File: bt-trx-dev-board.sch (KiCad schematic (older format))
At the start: 12 parts, among them J1 RJ45, J2 PTT_BUTTON, J3 PTT_CON, J5 PTT_SELECT, U1 SILabs_WT32i

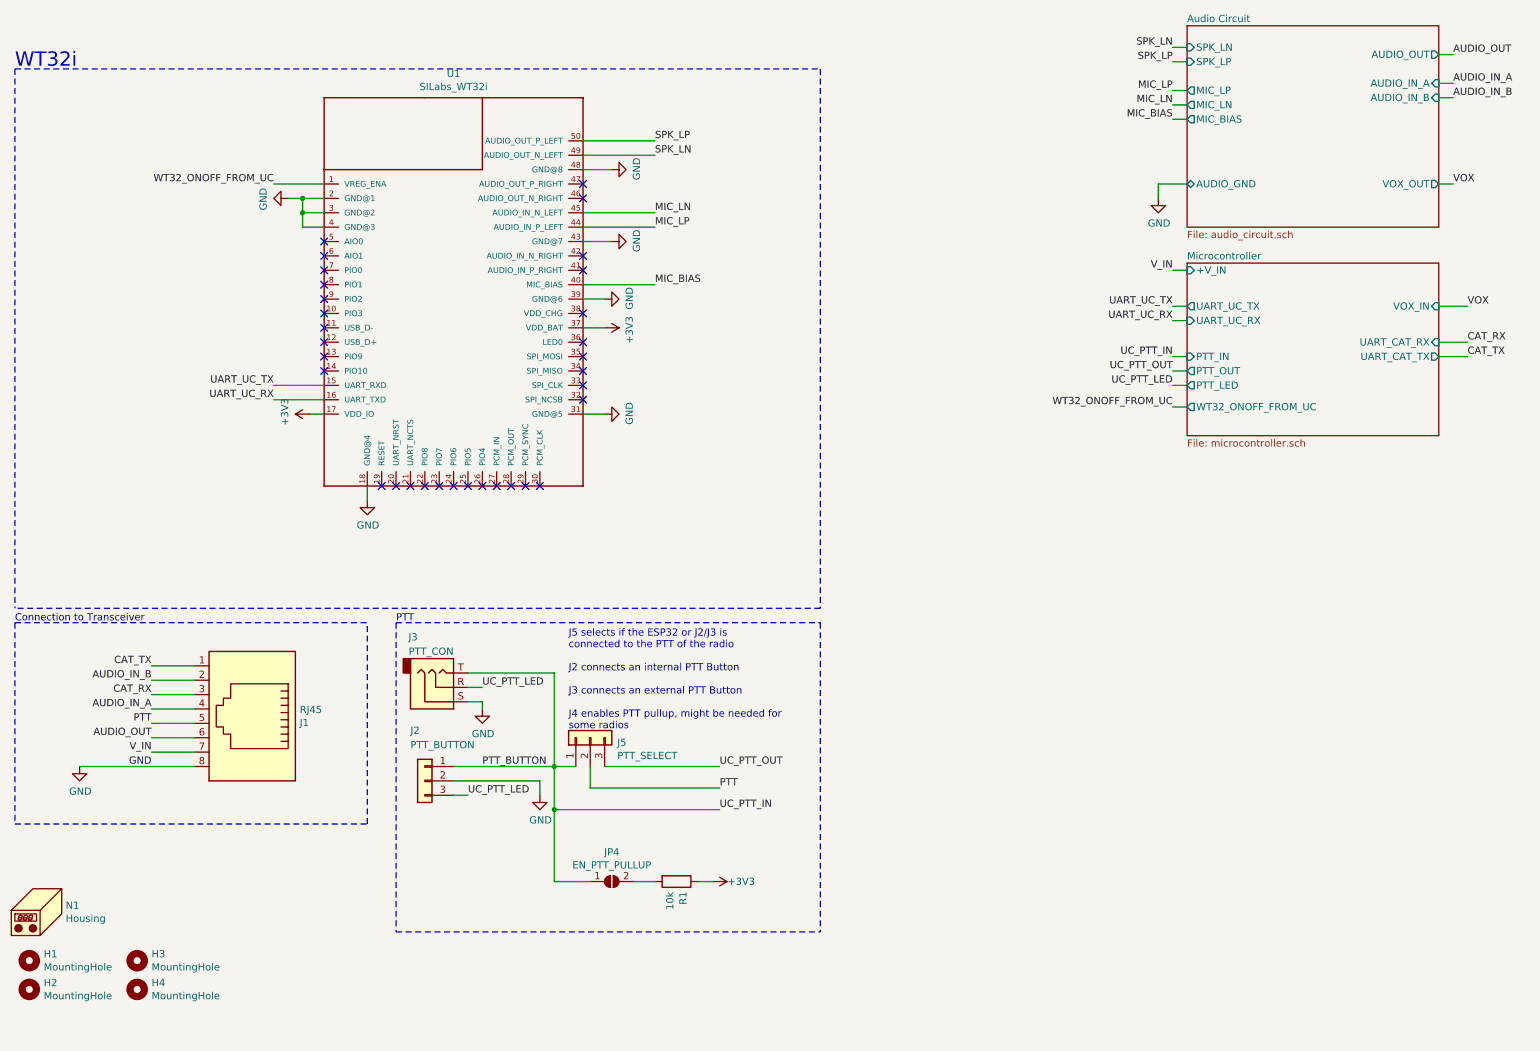
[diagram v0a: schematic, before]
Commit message: [#22] Insert Optocoupler for PTT
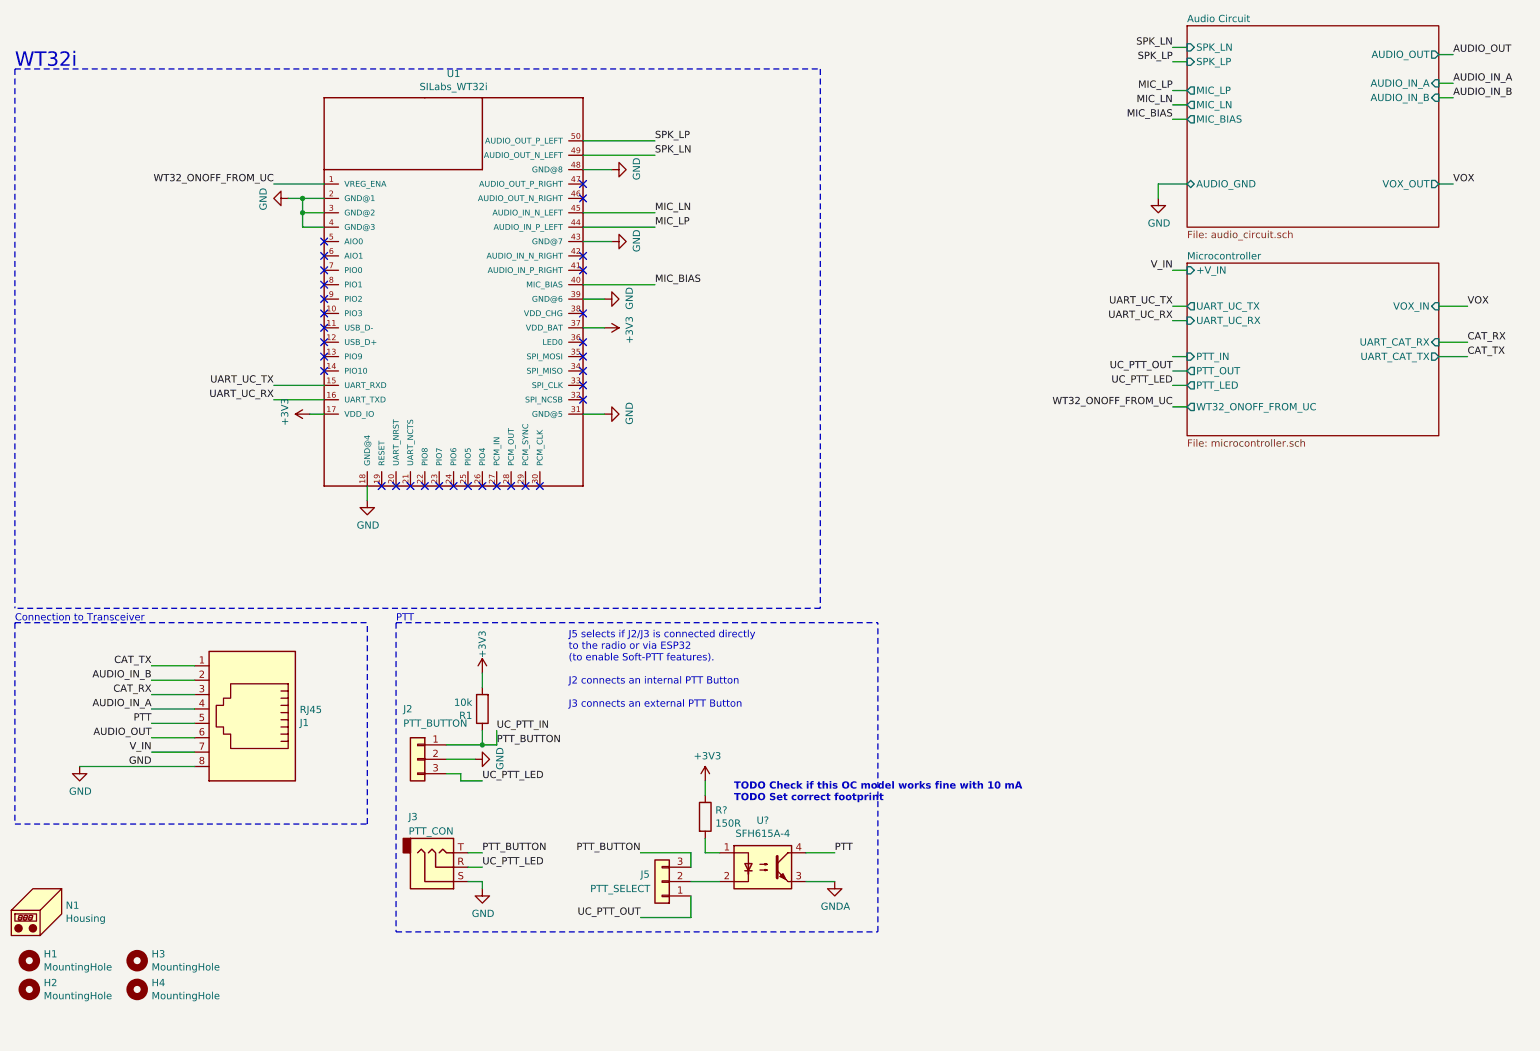
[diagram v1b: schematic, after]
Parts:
- removed JP4: EN_PTT_PULLUP, Jumper:SolderJumper-2_P1.3mm_Open_TrianglePad1.0x1.5mm, symbol Jumper:SolderJumper_2_Open
- added R?: 150R, Resistor_SMD:R_0805_2012Metric_Pad1.15x1.40mm_HandSolder, symbol Device:R
- added U?: SFH615A-4, Package_DIP:DIP-4_W7.62mm, symbol Isolator:SFH617A-1
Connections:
- net +3V3: now also R1.2, R?.1; no longer R1.1
- net PTT: now also U?.4; no longer J5.2 (Pin_2)
- net PTT_BUTTON: now also J5.3 (Pin_3), R1.1; no longer J5.1 (Pin_1)
- net UC_PTT_OUT: now also J5.1 (Pin_1); no longer J5.3 (Pin_3)
- new net: J5.2 (Pin_2), U?.2
- new net: R?.2, U?.1
- new net GNDA: U?.3
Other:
- note added: "J5 selects if J2/J3 is connected directly\nto the radio or via ESP32\n(to enable Soft-PTT features).\n\nJ2 connects an internal PTT Button\n\nJ3 connects an external PTT Button"
- note added: "TODO Check if this OC model works fine with 10 mA\nTODO Set correct footprint"
- note removed: "J5 selects if the ESP32 or J2/J3 is\nconnected to the PTT of the radio\n\nJ2 connects an internal PTT Button\n\nJ3 connects an external PTT Button\n\nJ4 enables PTT pullup, might be needed for\nsome radios"
- moved on the sheet: J2, J3, J5, R1
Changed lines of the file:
@@
 Sheet 1 3
 Title "BT-TRX Development Board "
-Date "2019-09-28"
-Rev "v4.1"
+Date "2020-01-04"
+Rev "v5.0"
 Comp "bt-trx.com"
 Comment1 "Licensed under CERN OHL v1.2 - https://ohwr.org/licenses/cern-ohl/v1.2"
@@
 L power:GND #PWR05
 U 1 1 5C0EA10B
-P 4350 6000
-F 0 "#PWR05" H 4350 5750 50  0001 C CNN
-F 1 "GND" H 4355 5827 50  0000 C CNN
-F 2 "" H 4350 6000 50  0001 C CNN
-F 3 "" H 4350 6000 50  0001 C CNN
-	1    4350 6000
-	1    0    0    -1
+P 3900 5750
+F 0 "#PWR05" H 3900 5500 50  0001 C CNN
+F 1 "GND" H 3905 5577 50  0000 C CNN
+F 2 "" H 3900 5750 50  0001 C CNN
+F 3 "" H 3900 5750 50  0001 C CNN
+	1    3900 5750
+	0    -1   -1   0
 $EndComp
 $Comp
@@
 L Connector_Generic:Conn_01x03 J5
 U 1 1 5C7B53A0
-P 4700 5600
-F 0 "J5" V 4666 5412 50  0000 R CNN
-F 1 "PTT_SELECT" V 4575 5412 50  0000 R CNN
-F 2 "Connector_PinHeader_2.54mm:PinHeader_1x03_P2.54mm_Vertical" H 4700 5600 50  0001 C CNN
-F 3 "~" H 4700 5600 50  0001 C CNN
-F 4 "855-M20-9990346" H -2200 -200 50  0001 C CNN "Mouser Best.Nr."
-	1    4700 5600
-	0    -1   -1   0
-$EndComp
-Wire Wire Line
-	4800 5800 5600 5800
-Text Label 5600 5800 0    50   ~ 0
+P 5200 6600
+F 0 "J5" H 5350 6550 50  0000 R CNN
+F 1 "PTT_SELECT" H 5700 6650 50  0000 R CNN
+F 2 "Connector_PinHeader_2.54mm:PinHeader_1x03_P2.54mm_Vertical" H 5200 6600 50  0001 C CNN
+F 3 "~" H 5200 6600 50  0001 C CNN
+F 4 "855-M20-9990346" H -1700 800 50  0001 C CNN "Mouser Best.Nr."
+	1    5200 6600
+	-1   0    0    1
+$EndComp
+Text Label 5050 6850 2    50   ~ 0
 UC_PTT_OUT
-Wire Wire Line
-	4700 5800 4700 5950
-Wire Wire Line
-	4700 5950 5600 5950
-Text Label 5600 5950 0    50   ~ 0
+Text Label 6400 6400 0    50   ~ 0
 PTT
-Text Label 3950 5800 0    50   ~ 0
+Text Label 4050 5650 0    50   ~ 0
 PTT_BUTTON
 $Sheet
@@
 Wire Wire Line
 	8850 3050 8750 3050
-Text Label 8750 2950 2    50   ~ 0
-UC_PTT_IN
 Text Label 8750 3050 2    50   ~ 0
 UC_PTT_OUT
-Connection ~ 4450 5800
-Wire Wire Line
-	4450 5800 4600 5800
 $Comp
 L power:GND #PWR06
 U 1 1 5C7A36F0
-P 3950 5400
-F 0 "#PWR06" H 3950 5150 50  0001 C CNN
-F 1 "GND" H 3955 5227 50  0000 C CNN
-F 2 "" H 3950 5400 50  0001 C CNN
-F 3 "" H 3950 5400 50  0001 C CNN
-	1    3950 5400
-	1    0    0    -1
-$EndComp
-Wire Wire Line
-	3950 5350 3950 5400
-Wire Wire Line
-	3850 5350 3950 5350
-Wire Wire Line
-	4450 5150 4450 5800
+P 3950 6650
+F 0 "#PWR06" H 3950 6400 50  0001 C CNN
+F 1 "GND" H 3955 6477 50  0000 C CNN
+F 2 "" H 3950 6650 50  0001 C CNN
+F 3 "" H 3950 6650 50  0001 C CNN
+	1    3950 6650
+	1    0    0    -1
+$EndComp
+Wire Wire Line
+	3950 6600 3950 6650
+Wire Wire Line
+	3850 6600 3950 6600
 $Comp
 L power:GND #PWR01
@@
 L power:+3V3 #PWR012
 U 1 1 5CD1BCEE
-P 5550 6600
+P 3950 5150
 AR Path="/5CD1BCEE" Ref="#PWR012"  Part="1"
 AR Path="/5C10B93A/5CD1BCEE" Ref="#PWR?"  Part="1"
-F 0 "#PWR012" H 5550 6450 50  0001 C CNN
-F 1 "+3V3" V 5550 6800 50  0000 C CNN
-F 2 "" H 5550 6600 50  0001 C CNN
-F 3 "" H 5550 6600 50  0001 C CNN
-	1    5550 6600
-	0    1    1    0
+F 0 "#PWR012" H 3950 5000 50  0001 C CNN
+F 1 "+3V3" V 3950 5350 50  0000 C CNN
+F 2 "" H 3950 5150 50  0001 C CNN
+F 3 "" H 3950 5150 50  0001 C CNN
+	1    3950 5150
+	1    0    0    -1
 $EndComp
 $Comp
 L Device:R R1
 U 1 1 5CD1BCF6
-P 5300 6600
+P 3950 5400
 AR Path="/5CD1BCF6" Ref="R1"  Part="1"
 AR Path="/5C10B93A/5CD1BCF6" Ref="R?"  Part="1"
-F 0 "R1" H 5370 6646 50  0000 L CNN
-F 1 "10k" H 5370 6555 50  0000 L CNN
-F 2 "Resistor_SMD:R_0805_2012Metric_Pad1.15x1.40mm_HandSolder" V 5230 6600 50  0001 C CNN
-F 3 "~" H 5300 6600 50  0001 C CNN
-F 4 " 603-RC0805FR-0710KL" H 1650 1450 50  0001 C CNN "Mouser Best.Nr."
-	1    5300 6600
-	0    1    1    0
-$EndComp
-Wire Wire Line
-	5550 6600 5450 6600
-Text Label 5600 6100 0    50   ~ 0
-UC_PTT_IN
-Text Notes 4550 5550 0    50   ~ 0
-J5 selects if the ESP32 or J2/J3 is\nconnected to the PTT of the radio\n\nJ2 connects an internal PTT Button\n\nJ3 connects an external PTT Button\n\nJ4 enables PTT pullup, might be needed for\nsome radios
-Wire Notes Line
-	3350 6950 6300 6950
-Wire Notes Line
-	3350 4800 6300 4800
+F 0 "R1" H 4020 5446 50  0000 L CNN
+F 1 "10k" H 4020 5355 50  0000 L CNN
+F 2 "Resistor_SMD:R_0805_2012Metric_Pad1.15x1.40mm_HandSolder" V 3880 5400 50  0001 C CNN
+F 3 "~" H 3950 5400 50  0001 C CNN
+F 4 " 603-RC0805FR-0710KL" H 300 250 50  0001 C CNN "Mouser Best.Nr."
+	1    3950 5400
+	-1   0    0    1
+$EndComp
+Text Notes 4550 5400 0    50   ~ 0
+J5 selects if J2/J3 is connected directly\nto the radio or via ESP32\n(to enable Soft-PTT features).\n\nJ2 connects an internal PTT Button\n\nJ3 connects an external PTT Button
 $Comp
 L Mechanical:MountingHole H3
@@
 	1    0    0    -1
 $EndComp
-Wire Wire Line
-	4450 5800 4450 6100
-Wire Wire Line
-	5600 6100 4450 6100
-Connection ~ 4450 6100
-Wire Wire Line
-	4450 6100 4450 6600
-Wire Notes Line
-	6300 4800 6300 6950
 Wire Notes Line
 	3350 4800 3350 6950
@@
 L Connector:AudioJack3 J3
 U 1 1 5D8E8C9D
-P 3650 5250
-F 0 "J3" H 3500 4900 50  0000 R CNN
-F 1 "PTT_CON" H 3750 5000 50  0000 R CNN
-F 2 "Connector_Audio:Jack_3.5mm_CUI_SJ1-3533NG_Horizontal" H 3650 5250 50  0001 C CNN
-F 3 "~" H 3650 5250 50  0001 C CNN
-F 4 "490-SJ1-3533NG" H 3650 5250 50  0001 C CNN "Mouser Best.Nr."
-	1    3650 5250
+P 3650 6500
+F 0 "J3" H 3500 6150 50  0000 R CNN
+F 1 "PTT_CON" H 3750 6250 50  0000 R CNN
+F 2 "Connector_Audio:Jack_3.5mm_CUI_SJ1-3533NG_Horizontal" H 3650 6500 50  0001 C CNN
+F 3 "~" H 3650 6500 50  0001 C CNN
+F 4 "490-SJ1-3533NG" H 3650 6500 50  0001 C CNN "Mouser Best.Nr."
+	1    3650 6500
 	1    0    0    1
 $EndComp
 Wire Wire Line
-	3850 5250 3950 5250
-Text Label 3950 5250 0    50   ~ 0
+	3850 6500 3950 6500
+Text Label 3950 6500 0    50   ~ 0
 UC_PTT_LED
 Wire Wire Line
@@
 UC_PTT_LED
 Wire Wire Line
-	3850 5150 4450 5150
-Wire Wire Line
-	3750 5800 4450 5800
-Wire Wire Line
 	10600 2600 10800 2600
 Text Label 10800 2600 0    50   ~ 0
@@
 VOX
 $Comp
-L Jumper:SolderJumper_2_Open JP4
-U 1 1 5D933957
-P 4850 6600
-F 0 "JP4" H 4850 6805 50  0000 C CNN
-F 1 "EN_PTT_PULLUP" H 4850 6714 50  0000 C CNN
-F 2 "Jumper:SolderJumper-2_P1.3mm_Open_TrianglePad1.0x1.5mm" H 4850 6600 50  0001 C CNN
-F 3 "~" H 4850 6600 50  0001 C CNN
-	1    4850 6600
-	1    0    0    -1
-$EndComp
-Wire Wire Line
-	4450 6600 4700 6600
-Wire Wire Line
-	5000 6600 5150 6600
-$Comp
 L Connector_Generic:Conn_01x03 J2
 U 1 1 5D9A6771
-P 3550 5900
-F 0 "J2" H 3650 6250 50  0000 R CNN
-F 1 "PTT_BUTTON" H 3650 6150 50  0000 R CNN
-F 2 "Connector_PinHeader_2.54mm:PinHeader_1x03_P2.54mm_Vertical" H 3550 5900 50  0001 C CNN
-F 3 "~" H 3550 5900 50  0001 C CNN
-F 4 "855-M20-9990346" H -3350 100 50  0001 C CNN "Mouser Best.Nr."
-	1    3550 5900
+P 3500 5750
+F 0 "J2" H 3600 6100 50  0000 R CNN
+F 1 "PTT_BUTTON" H 3600 6000 50  0000 R CNN
+F 2 "Connector_PinHeader_2.54mm:PinHeader_1x03_P2.54mm_Vertical" H 3500 5750 50  0001 C CNN
+F 3 "~" H 3500 5750 50  0001 C CNN
+F 4 "855-M20-9990346" H -3400 -50 50  0001 C CNN "Mouser Best.Nr."
+	1    3500 5750
 	-1   0    0    -1
 $EndComp
-Text Label 3850 6000 0    50   ~ 0
+Text Label 3950 5900 0    50   ~ 0
 UC_PTT_LED
-Wire Wire Line
-	4350 5900 4350 6000
-Wire Wire Line
-	3750 5900 4350 5900
-Wire Wire Line
-	3750 6000 3850 6000
+$Comp
+L Isolator:SFH617A-1 U?
+U 1 1 5E115F72
+P 5900 6500
+F 0 "U?" H 5900 6825 50  0000 C CNN
+F 1 "SFH615A-4" H 5900 6734 50  0000 C CNN
+F 2 "Package_DIP:DIP-4_W7.62mm" H 5700 6300 50  0001 L CIN
+F 3 "https://asset.conrad.com/media10/add/160267/c1/-/en/000183258DS01/datenblatt-183258-isocom-components-optokoppler-phototransistor-sfh615a-4xsm-smd-4-transistor-dc.pdf" H 5900 6500 50  0001 L CNN
+	1    5900 6500
+	1    0    0    -1
+$EndComp
+$Comp
+L power:+3V3 #PWR0102
+U 1 1 5E11C622
+P 5500 5900
+F 0 "#PWR0102" H 5500 5750 50  0001 C CNN
+F 1 "+3V3" H 5515 6073 50  0000 C CNN
+F 2 "" H 5500 5900 50  0001 C CNN
+F 3 "" H 5500 5900 50  0001 C CNN
+	1    5500 5900
+	1    0    0    -1
+$EndComp
+$Comp
+L Device:R R?
+U 1 1 5E1205EF
+P 5500 6150
+AR Path="/5E1205EF" Ref="R?"  Part="1"
+AR Path="/5C10B93A/5E1205EF" Ref="R?"  Part="1"
+F 0 "R?" H 5570 6196 50  0000 L CNN
+F 1 "150R" H 5570 6105 50  0000 L CNN
+F 2 "Resistor_SMD:R_0805_2012Metric_Pad1.15x1.40mm_HandSolder" V 5430 6150 50  0001 C CNN
+F 3 "~" H 5500 6150 50  0001 C CNN
+F 4 " 603-RC0805FR-0710KL" H 1850 1000 50  0001 C CNN "Mouser Best.Nr."
+	1    5500 6150
+	1    0    0    -1
+$EndComp
+Wire Wire Line
+	5500 5900 5500 6000
+Wire Wire Line
+	5500 6300 5500 6400
+Wire Wire Line
+	5500 6400 5600 6400
+Wire Wire Line
+	5400 6600 5600 6600
+Wire Wire Line
+	5050 6850 5400 6850
+Wire Wire Line
+	5400 6850 5400 6700
+Wire Wire Line
+	3700 5750 3900 5750
+Wire Wire Line
+	3950 5650 3700 5650
+Text Label 3950 6400 0    50   ~ 0
+PTT_BUTTON
+Wire Wire Line
+	3700 5850 3800 5850
+Wire Wire Line
+	3950 5900 3800 5900
+Wire Wire Line
+	3800 5900 3800 5850
+Wire Wire Line
+	3850 6400 3950 6400
+Wire Wire Line
+	6200 6400 6400 6400
+Text Label 5050 6400 2    50   ~ 0
+PTT_BUTTON
+Wire Wire Line
+	5050 6400 5400 6400
+Wire Wire Line
+	5400 6400 5400 6500
+Wire Wire Line
+	3950 5150 3950 5250
+Wire Wire Line
+	3950 5550 3950 5650
+Wire Notes Line
+	6700 6950 6700 4800
+Wire Notes Line
+	3350 6950 6700 6950
+Wire Notes Line
+	3350 4800 6700 4800
+$Comp
+L power:GNDA #PWR0103
+U 1 1 5E1B9556
+P 6400 6600
+F 0 "#PWR0103" H 6400 6350 50  0001 C CNN
+F 1 "GNDA" H 6405 6427 50  0000 C CNN
+F 2 "" H 6400 6600 50  0001 C CNN
+F 3 "" H 6400 6600 50  0001 C CNN
+	1    6400 6600
+	1    0    0    -1
+$EndComp
+Wire Wire Line
+	6200 6600 6400 6600
+Text Notes 5700 6050 0    50   ~ 10
+TODO Check if this OC model works fine with 10 mA\nTODO Set correct footprint
+Text Label 4050 5550 0    50   ~ 0
+UC_PTT_IN
+Wire Wire Line
+	3950 5650 4050 5650
+Connection ~ 3950 5650
+Wire Wire Line
+	4050 5550 4050 5650
 $EndSCHEMATC

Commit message: [#23] Remove AUDIO_IN_B
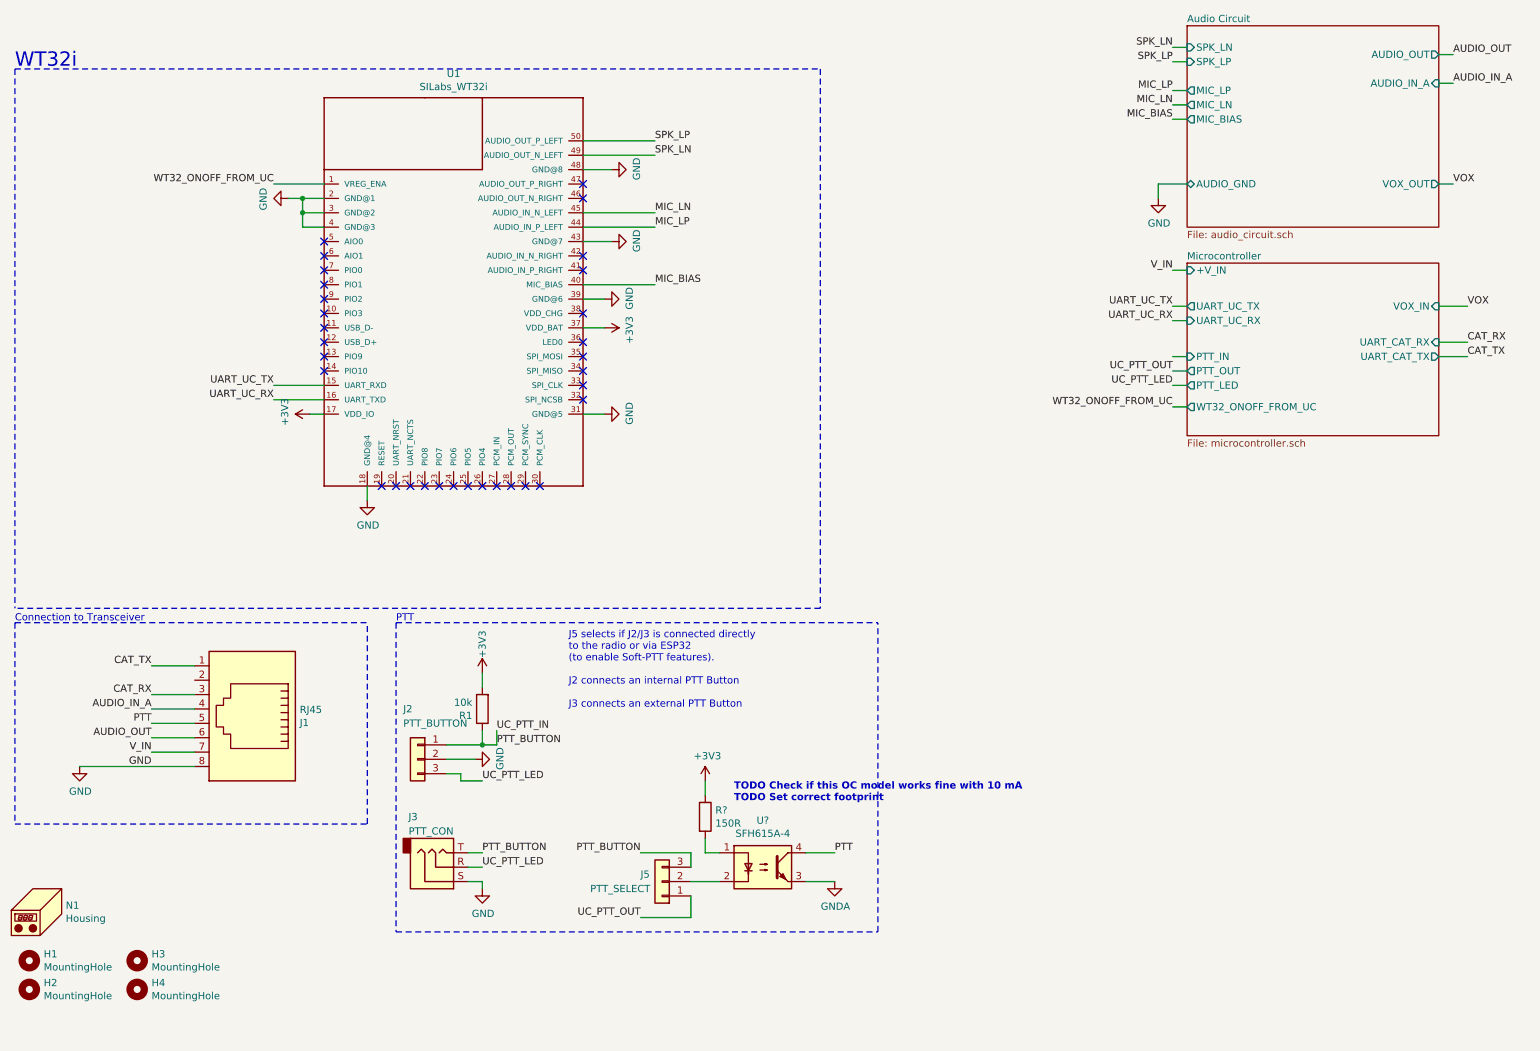
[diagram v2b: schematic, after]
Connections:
- net AUDIO_IN_B: no longer names the net of J1.2
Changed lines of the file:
@@
 Text Label 10700 1050 0    50   ~ 0
 AUDIO_IN_A
-Text Label 1650 5200 2    50   ~ 0
-AUDIO_IN_B
 Text Label 1650 5500 2    50   ~ 0
 PTT
@@
 Wire Wire Line
 	1650 5300 1950 5300
-Wire Wire Line
-	1650 5200 1950 5200
 Text Label 1650 5100 2    50   ~ 0
 CAT_TX
@@
 Text Notes 3350 4800 0    50   ~ 0
 PTT
-Wire Wire Line
-	10600 1150 10700 1150
-Text Label 10700 1150 0    50   ~ 0
-AUDIO_IN_B
 $Comp
 L power:GND #PWR05
@@
 F7 "AUDIO_IN_A" I R 10600 1050 50
 F8 "AUDIO_GND" B L 8850 1750 50
-F9 "AUDIO_IN_B" I R 10600 1150 50
-F10 "SPK_LP" I L 8850 900 50
-F11 "VOX_OUT" O R 10600 1750 50
+F9 "SPK_LP" I L 8850 900 50
+F10 "VOX_OUT" O R 10600 1750 50
 $EndSheet
 Wire Wire Line
